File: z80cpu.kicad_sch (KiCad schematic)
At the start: 7 parts

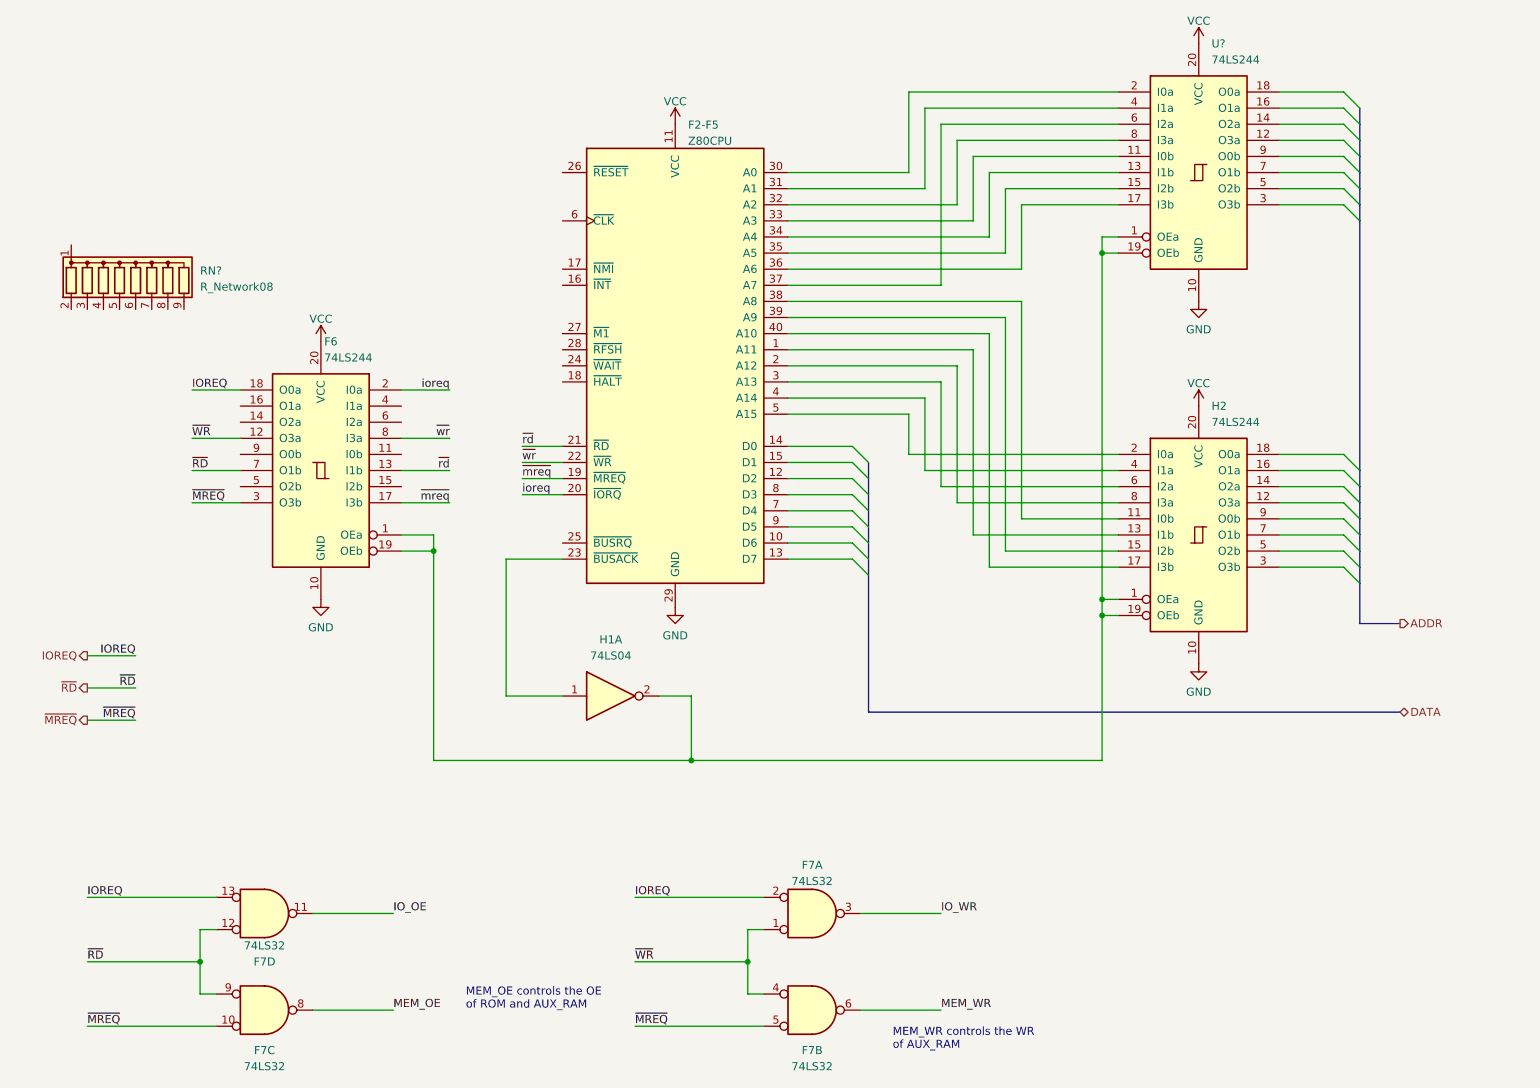
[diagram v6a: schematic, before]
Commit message: Z80 halt controls the RUN LED
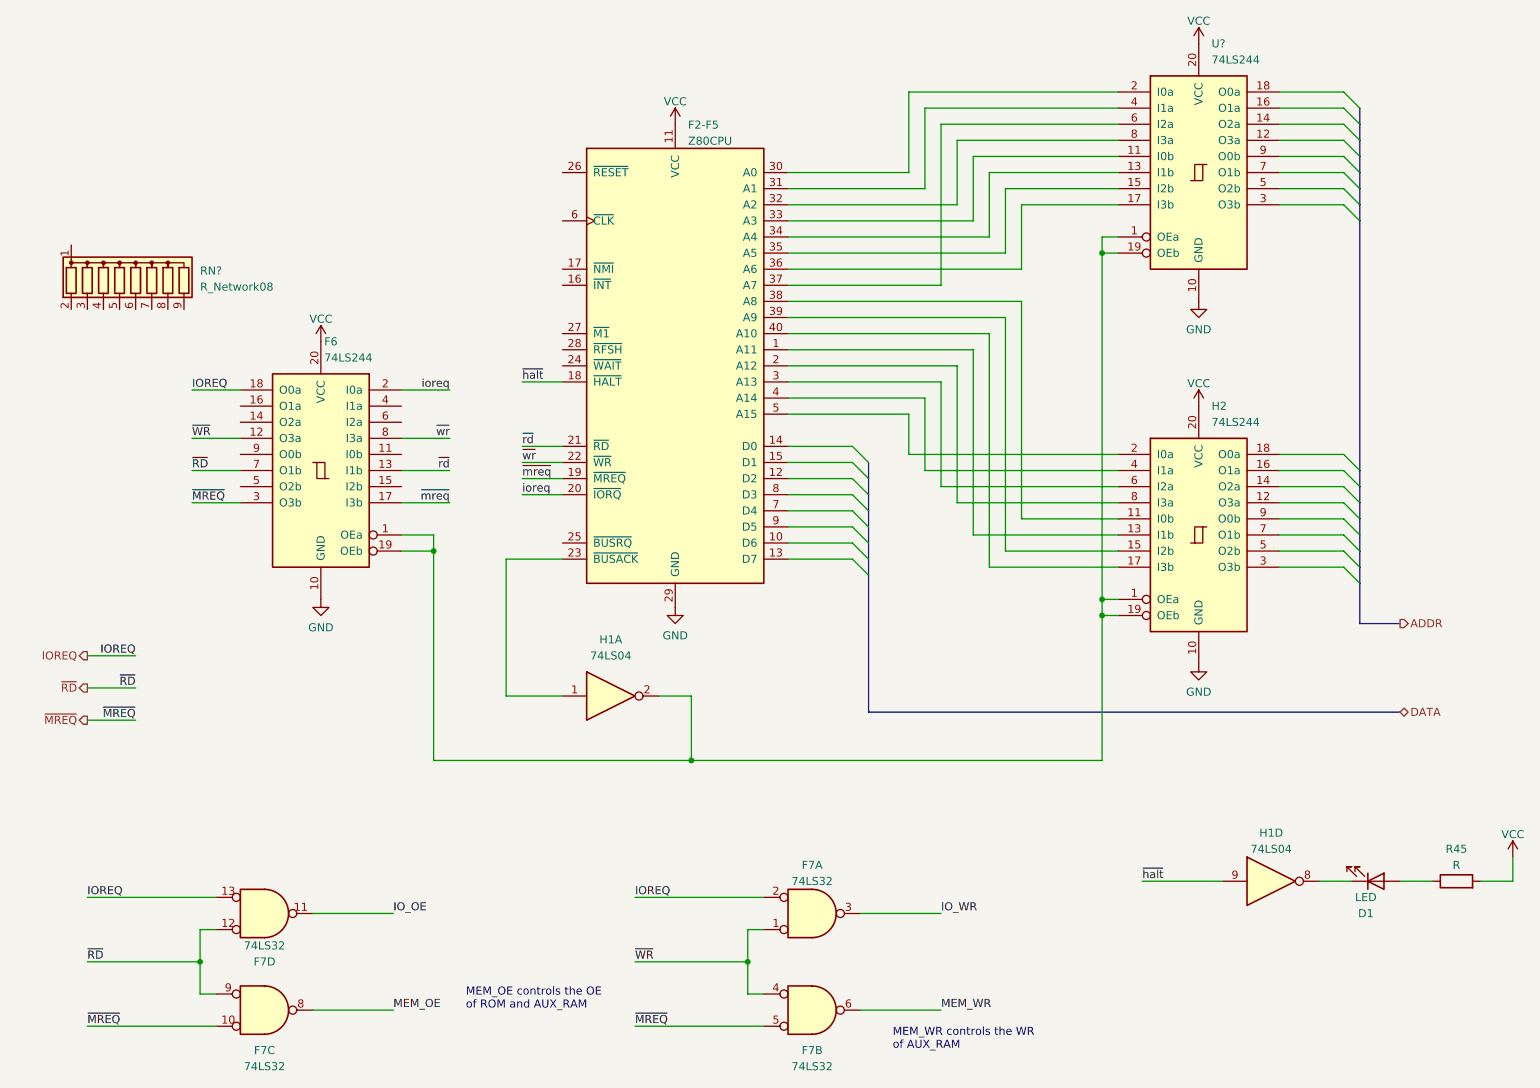
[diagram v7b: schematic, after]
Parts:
- added D1: LED, symbol Device:LED
- added unit 4 of H1
- added R45: R, symbol Device:R
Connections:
- net VCC: now also R45.2
- net ~{halt}: now reaches F2-F5.18 (~{HALT})
- net ~{halt}: now also H1.9
- new net: D1.2 (A), R45.1
- new net: D1.1 (K), H1.8
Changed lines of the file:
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@@
+    (stroke (width 0) (type default))
+  )
+  (wire (pts (xy 91.44 74.93) (xy 97.79 74.93))
     (stroke (width 0) (type default))
   )
@@
     (stroke (width 0) (type default))
   )
+  (wire (pts (xy 242.57 153.67) (xy 247.65 153.67))
+    (stroke (width 0) (type default))
+  )
   (bus (pts (xy 146.05 102.87) (xy 146.05 105.41))
     (stroke (width 0) (type default))
@@
     (stroke (width 0) (type default))
   )
+  (wire (pts (xy 217.17 153.67) (xy 222.25 153.67))
+    (stroke (width 0) (type default))
+  )
   (wire (pts (xy 72.39 99.06) (xy 77.47 99.06))
     (stroke (width 0) (type default))
@@
     (stroke (width 0) (type default))
   )
+  (wire (pts (xy 247.65 149.86) (xy 247.65 153.67))
+    (stroke (width 0) (type default))
+  )
   (wire (pts (xy 182.88 111.76) (xy 185.42 111.76))
     (stroke (width 0) (type default))
@@
     (stroke (width 0) (type default))
   )
+  (wire (pts (xy 229.87 153.67) (xy 234.95 153.67))
+    (stroke (width 0) (type default))
+  )
   (wire (pts (xy 133.35 44.45) (xy 154.94 44.45))
     (stroke (width 0) (type default))
@@
     (stroke (width 0) (type default))
   )
+  (wire (pts (xy 189.23 153.67) (xy 201.93 153.67))
+    (stroke (width 0) (type default))
+  )
   (wire (pts (xy 133.35 95.25) (xy 143.51 95.25))
     (stroke (width 0) (type default))
@@
   )
   (label "MEM_WR" (at 157.48 173.99 0) (fields_autoplaced)
+    (effects (font (size 1.27 1.27)) (justify left bottom))
+  )
+  (label "~{halt}" (at 91.44 74.93 0) (fields_autoplaced)
     (effects (font (size 1.27 1.27)) (justify left bottom))
   )
@@
   )
   (label "IOREQ" (at 39.37 76.2 0) (fields_autoplaced)
+    (effects (font (size 1.27 1.27)) (justify left bottom))
+  )
+  (label "~{halt}" (at 189.23 153.67 0) (fields_autoplaced)
     (effects (font (size 1.27 1.27)) (justify left bottom))
   )
@@
         (path "/12a6dbe3-008d-4c5b-88f6-9f1c816060be/1847fdc4-53d8-4940-8c5f-7a326599bae2"
           (reference "#PWR?") (unit 1)
+        )
+      )
+    )
+  )
+  (symbol (lib_id "Device:R") (at 238.76 153.67 90) (unit 1)
+    (in_bom yes) (on_board yes) (dnp no) (fields_autoplaced)
+    (property "Reference" "R45" (at 238.76 148.59 90)
+      (effects (font (size 1.27 1.27)))
+    )
+    (property "Value" "R" (at 238.76 151.13 90)
+      (effects (font (size 1.27 1.27)))
+    )
+    (property "Footprint" "" (at 238.76 155.448 90)
+      (effects (font (size 1.27 1.27)) hide)
+    )
+    (property "Datasheet" "~" (at 238.76 153.67 0)
+      (effects (font (size 1.27 1.27)) hide)
+    )
+    (pin "1")
+    (pin "2")
+    (instances
+      (project "ceda"
+        (path "/12a6dbe3-008d-4c5b-88f6-9f1c816060be/1847fdc4-53d8-4940-8c5f-7a326599bae2"
+          (reference "R45") (unit 1)
         )
       )
@@
     )
   )
+  (symbol (lib_id "74xx:74LS04") (at 209.55 153.67 0) (unit 4)
+    (in_bom yes) (on_board yes) (dnp no) (fields_autoplaced)
+    (property "Reference" "H1" (at 209.55 146.05 0)
+      (effects (font (size 1.27 1.27)))
+    )
+    (property "Value" "74LS04" (at 209.55 148.59 0)
+      (effects (font (size 1.27 1.27)))
+    )
+    (property "Footprint" "" (at 209.55 153.67 0)
+      (effects (font (size 1.27 1.27)) hide)
+    )
+    (property "Datasheet" "http://www.ti.com/lit/gpn/sn74LS04" (at 209.55 153.67 0)
+      (effects (font (size 1.27 1.27)) hide)
+    )
+    (pin "1")
+    (pin "2")
+    (pin "3")
+    (pin "4")
+    (pin "5")
+    (pin "6")
+    (pin "8")
+    (pin "9")
+    (pin "10")
+    (pin "11")
+    (pin "12")
+    (pin "13")
+    (pin "14")
+    (pin "7")
+    (instances
+      (project "ceda"
+        (path "/12a6dbe3-008d-4c5b-88f6-9f1c816060be/1847fdc4-53d8-4940-8c5f-7a326599bae2"
+          (reference "H1") (unit 4)
+        )
+      )
+    )
+  )
   (symbol (lib_id "power:VCC") (at 59.69 68.58 0) (unit 1)
     (in_bom yes) (on_board yes) (dnp no) (fields_autoplaced)
@@
         (path "/12a6dbe3-008d-4c5b-88f6-9f1c816060be/1847fdc4-53d8-4940-8c5f-7a326599bae2"
           (reference "#PWR?") (unit 1)
+        )
+      )
+    )
+  )
+  (symbol (lib_id "Device:LED") (at 226.06 153.67 0) (mirror x) (unit 1)
+    (in_bom yes) (on_board yes) (dnp no)
+    (property "Reference" "D1" (at 224.4725 158.75 0)
+      (effects (font (size 1.27 1.27)))
+    )
+    (property "Value" "LED" (at 224.4725 156.21 0)
+      (effects (font (size 1.27 1.27)))
+    )
+    (property "Footprint" "" (at 226.06 153.67 0)
+      (effects (font (size 1.27 1.27)) hide)
+    )
+    (property "Datasheet" "~" (at 226.06 153.67 0)
+      (effects (font (size 1.27 1.27)) hide)
+    )
+    (pin "1")
+    (pin "2")
+    (instances
+      (project "ceda"
+        (path "/12a6dbe3-008d-4c5b-88f6-9f1c816060be/1847fdc4-53d8-4940-8c5f-7a326599bae2"
+          (reference "D1") (unit 1)
         )
       )
@@
         )
       )
+    )
+  )
+  (symbol (lib_id "power:VCC") (at 247.65 149.86 0) (unit 1)
+    (in_bom yes) (on_board yes) (dnp no) (fields_autoplaced)
+    (property "Reference" "#PWR04" (at 247.65 153.67 0)
+      (effects (font (size 1.27 1.27)) hide)
+    )
+    (property "Value" "VCC" (at 247.65 146.2842 0)
+      (effects (font (size 1.27 1.27)))
+    )
+    (property "Footprint" "" (at 247.65 149.86 0)
+      (effects (font (size 1.27 1.27)) hide)
+    )
+    (property "Datasheet" "" (at 247.65 149.86 0)
+      (effects (font (size 1.27 1.27)) hide)
+    )
+    (pin "1")
+    (instances
+      (project "ceda"
+        (path "/12a6dbe3-008d-4c5b-88f6-9f1c816060be/1847fdc4-53d8-4940-8c5f-7a326599bae2"
+          (reference "#PWR04") (unit 1)
+        )
+      )

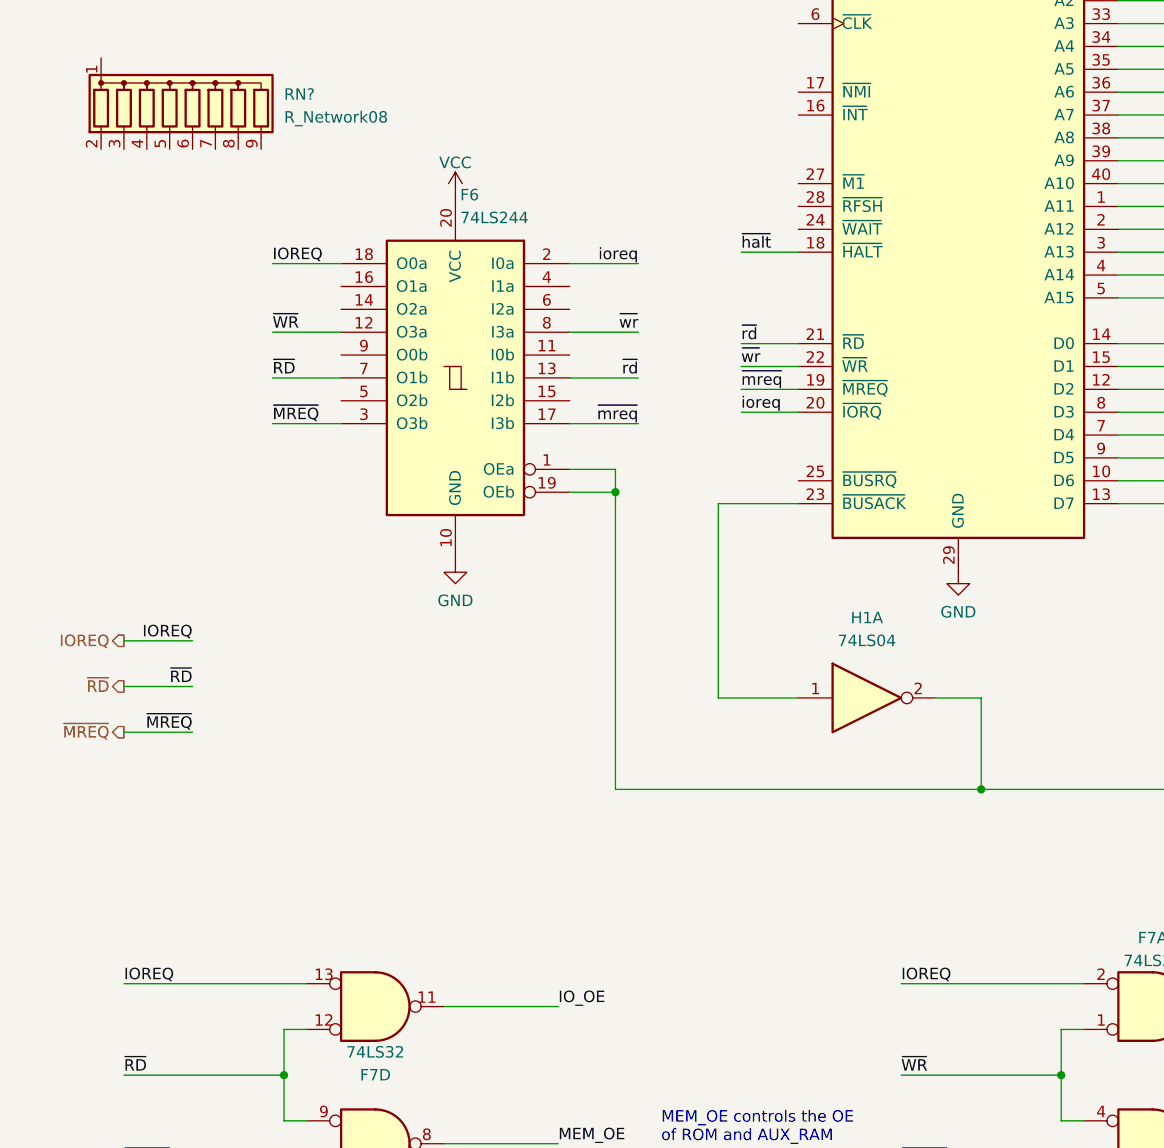
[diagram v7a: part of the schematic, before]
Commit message: Partial signal renaming
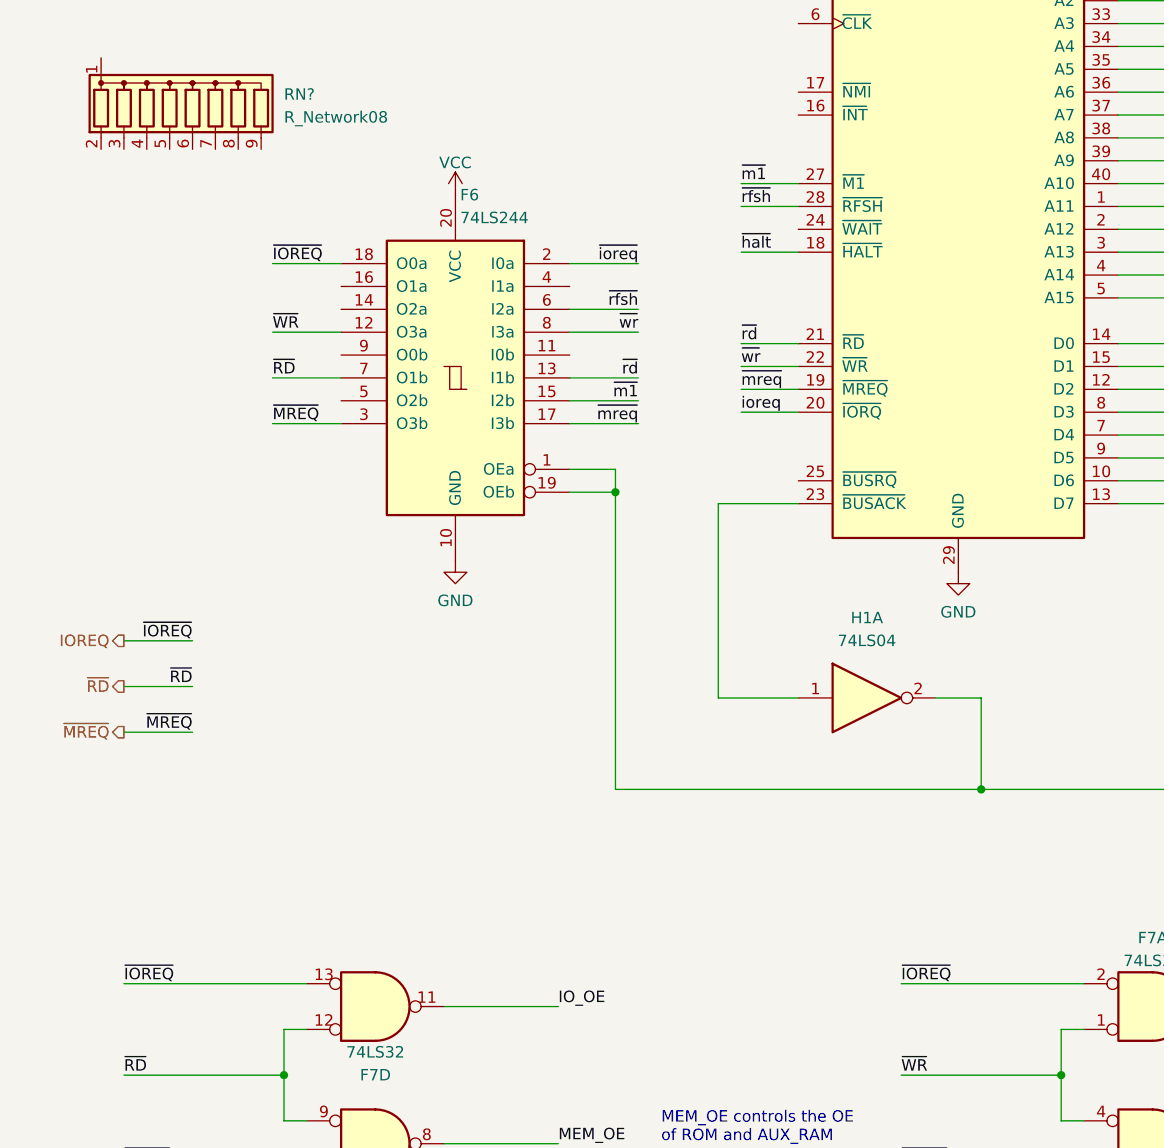
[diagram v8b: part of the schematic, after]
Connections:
- net ioreq: no longer F6.2 (I0a)
- net ~{m1}: now reaches F2-F5.27 (~{M1})
- net ~{m1}: now also F6.15 (I2b)
- net ~{rfsh}: now reaches F2-F5.28 (~{RFSH})
- net ~{rfsh}: now also F6.6 (I2a)
- new net ~{ioreq}: F6.2 (I0a)
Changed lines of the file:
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@@
+    (stroke (width 0) (type default))
+  )
+  (wire (pts (xy 91.44 67.31) (xy 97.79 67.31))
     (stroke (width 0) (type default))
   )
@@
     (stroke (width 0) (type default))
   )
+  (wire (pts (xy 72.39 81.28) (xy 80.01 81.28))
+    (stroke (width 0) (type default))
+  )
   (wire (pts (xy 154.94 88.9) (xy 185.42 88.9))
     (stroke (width 0) (type default))
@@
     (stroke (width 0) (type default))
   )
+  (wire (pts (xy 91.44 69.85) (xy 97.79 69.85))
+    (stroke (width 0) (type default))
+  )
   (wire (pts (xy 157.48 34.29) (xy 157.48 59.69))
     (stroke (width 0) (type default))
@@
     (stroke (width 0) (type default))
   )
+  (wire (pts (xy 72.39 91.44) (xy 80.01 91.44))
+    (stroke (width 0) (type default))
+  )
   (bus (pts (xy 146.05 92.71) (xy 146.05 95.25))
     (stroke (width 0) (type default))
@@
     (effects (font (size 1.27 1.27)) (justify left bottom))
   )
-  (label "ioreq" (at 80.01 76.2 180) (fields_autoplaced)
+  (label "~{ioreq}" (at 80.01 76.2 180) (fields_autoplaced)
     (effects (font (size 1.27 1.27)) (justify right bottom))
   )
@@
     (effects (font (size 1.27 1.27)) (justify left bottom))
   )
-  (label "IOREQ" (at 39.37 76.2 0) (fields_autoplaced)
+  (label "~{IOREQ}" (at 39.37 76.2 0) (fields_autoplaced)
     (effects (font (size 1.27 1.27)) (justify left bottom))
   )
@@
     (effects (font (size 1.27 1.27)) (justify right bottom))
   )
-  (label "IOREQ" (at 30.48 118.11 180) (fields_autoplaced)
+  (label "~{m1}" (at 91.44 67.31 0) (fields_autoplaced)
+    (effects (font (size 1.27 1.27)) (justify left bottom))
+  )
+  (label "~{IOREQ}" (at 30.48 118.11 180) (fields_autoplaced)
     (effects (font (size 1.27 1.27)) (justify right bottom))
   )
@@
     (effects (font (size 1.27 1.27)) (justify left bottom))
   )
-  (label "IOREQ" (at 22.86 156.21 0) (fields_autoplaced)
+  (label "~{IOREQ}" (at 22.86 156.21 0) (fields_autoplaced)
     (effects (font (size 1.27 1.27)) (justify left bottom))
   )
@@
     (effects (font (size 1.27 1.27)) (justify right bottom))
   )
-  (label "IOREQ" (at 109.22 156.21 0) (fields_autoplaced)
-    (effects (font (size 1.27 1.27)) (justify left bottom))
-  )
+  (label "~{m1}" (at 80.01 91.44 180) (fields_autoplaced)
+    (effects (font (size 1.27 1.27)) (justify right bottom))
+  )
+  (label "~{rfsh}" (at 80.01 81.28 180) (fields_autoplaced)
+    (effects (font (size 1.27 1.27)) (justify right bottom))
+  )
+  (label "~{IOREQ}" (at 109.22 156.21 0) (fields_autoplaced)
+    (effects (font (size 1.27 1.27)) (justify left bottom))
+  )
+  (label "~{rfsh}" (at 91.44 69.85 0) (fields_autoplaced)
+    (effects (font (size 1.27 1.27)) (justify left bottom))
+  )
